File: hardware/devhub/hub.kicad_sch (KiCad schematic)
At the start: 32 parts, among them J2 USB-C UPSTREAM, U12 MCP120T-300I/TT, U2 USB2517I-JZX, Y1 24MHz 12pF

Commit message: Schematic: keep only host system LED, merge VBUS switches into hub sheet (D82, D83)
- remove relay LED (D90/R90) and power LED (D92/R92)
- move UCS2114 VBUS switches into the hub sheet, renamed to
  "Hub USB e switch VBUS"
- move the host LED into the MCU sheet as a local net
- drop the switches and ui sheets; update netclass patterns and docs
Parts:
- added C60, C63: 100n, Capacitor_SMD:C_0603_1608Metric, symbol Device:C
- added C61, C62, C64, C65: 1u 25V, Capacitor_SMD:C_0603_1608Metric, symbol Device:C
- added R60, R61: 27k 1%, Resistor_SMD:R_0603_1608Metric, symbol Device:R
- added R62, R63, R64, R65: 10k, Resistor_SMD:R_0603_1608Metric, symbol Device:R
- added U4, U5: UCS2114-1-V/LX, lcsc_footprints:UCS2114_VQFN-20_3x3mm_P0.5mm, symbol devhub:UCS2114
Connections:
- net +3V3: now also R62.1, R63.1, R64.1, R65.1
- net FAULT_P1: now also R62.2, U4.20 (~{ALERT1})
- net FAULT_P2: now also R63.2, U4.16 (~{ALERT2})
- net FAULT_P3: now also R64.2, U5.20 (~{ALERT1})
- net FAULT_P4: now also R65.2, U5.16 (~{ALERT2})
- net GND: now also C60.2, C61.2, C62.2, C63.2, C64.2, C65.2, R60.2, R61.2, U4.13 (~{BOOST}), U4.14 (GND), U4.17 (GND), U4.2 (GND), U5.13 (~{BOOST}), U5.14 (GND), U5.17 (GND), U5.2 (GND)
- net I2C1_SCL: now also U4.19 (SMCLK)
- net I2C1_SDA: now also U4.18 (SMDATA)
- new net +5V: C60.1, C61.1, C62.1, C63.1, C64.1, C65.1, U4.10 (VS), U4.6 (VS), U4.7 (VS), U4.8 (VDD), U4.9 (VS), U5.10 (VS), U5.6 (VS), U5.7 (VS), U5.8 (VDD), U5.9 (VS)
- new net EN_P1: U4.1 (PWR_EN1)
- new net EN_P2: U4.15 (PWR_EN2)
- new net EN_P3: U5.1 (PWR_EN1)
- new net EN_P4: U5.15 (PWR_EN2)
- new net I2C2_SCL: U5.19 (SMCLK)
- new net I2C2_SDA: U5.18 (SMDATA)
- new net ILIM_U4: R60.1, U4.3 (COMM_ILIM)
- new net ILIM_U5: R61.1, U5.3 (COMM_ILIM)
- new net VBUS_P1: U4.4 (VBUS1), U4.5 (VBUS1)
- new net VBUS_P2: U4.11 (VBUS2), U4.12 (VBUS2)
- new net VBUS_P3: U5.4 (VBUS1), U5.5 (VBUS1)
- new net VBUS_P4: U5.11 (VBUS2), U5.12 (VBUS2)
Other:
- note added: "Porte: 1-4 USB-C, 6 MCU (interna, non sezionabile); 5 e 7 non usate, disabilitate dal MCU via SMBus (con CFG_SEL 001 e 101 gli strap sono disattivati, D76). OCS1-4 dagli ALERT# degli UCS2114 (pull-up esterni R62-R65)."
- note added: "Switch VBUS delle porte: due UCS2114-1-V/LX (D75), U4 porte 1-2 su I2C1 e U5 porte 3-4 su I2C2, entrambi all'indirizzo 0x57. COMM_ILIM 27 k 1 %: modo SMBus, PWR_EN attivi alti, limite ILIM7 2,50-2,90 A per porta. Scarica VBUS automatica abilitata dal MCU all'avvio via SMBus (EN_VBUS_DISCHG, 400 ms): nessun GPIO di scarica. ALERT# open-drain con pull-up 10 k a 3,3 V: al MCU (FAULT_Px) e agli OCS1-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"
- note removed: "Porte: 1-4 USB-C, 6 MCU (interna, non sezionabile); 5 e 7 non usate, disabilitate dal MCU via SMBus (con CFG_SEL 001 e 101 gli strap sono disattivati, D76). OCS1-4 dagli ALERT# degli UCS2114 (pull-up esterni, foglio switches)."
- title: Hub USB 2.0 a 7 porte (USB2517) e porta upstream -> Hub USB2517, upstream e switch VBUS UCS2114

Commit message: PCB routing complete, package in values, MPN fields
- Routing finished; ESD_FANOUT rule area for D20 centre pins
- Vias keep inner-layer rings only where connected; GND reference vias
  next to SWD and I2C layer changes
- Value field of chip R/C/LED includes the package (0402...1206)
- New fields MPN lcsc, MPN mouser, MPN digikey; LCSC codes for R60/R61,
  U3, U4/U5 and supplier codes completed; JP2 marked DNP on the PCB
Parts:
- C20: value 4.7u -> 4.7u 0805; MPN digikey (none) -> CL21A475KOFNNNE; MPN lcsc (none) -> CL21A475KOFNNNE; MPN mouser (none) -> CL21A475KOFNNNE
- C21, C31, C32, C33, C35: value 1u -> 1u 0603; MPN digikey (none) -> CL10B105KA8NNNC; MPN lcsc (none) -> CL10B105KA8NNNC; MPN mouser (none) -> CL10B105KA8NNNC
- C22, C23: value 15p C0G -> 15p C0G 0603; MPN digikey (none) -> CL10C150JB8NNNC; MPN lcsc (none) -> CL10C150JB8NNNC; MPN mouser (none) -> CL10C150JB8NNNC
- C24, C60, C63: value 100n -> 100n 0603; MPN digikey (none) -> CL10B104KB8NNNC; MPN lcsc (none) -> CL10B104KB8NNNC; MPN mouser (none) -> CL10B104KB8NNNC
- C25, C26, C27, C28, C29, C30, C37, C38: value 100n -> 100n 0402; MPN digikey (none) -> CC0402KRX7R7BB104; MPN lcsc (none) -> CC0402KRX7R7BB104; MPN mouser (none) -> CC0402KRX7R7BB104
- C61, C62, C64, C65: value 1u 25V -> 1u 25V 0603; MPN digikey (none) -> CL10B105KA8NNNC; MPN lcsc (none) -> CL10B105KA8NNNC; MPN mouser (none) -> CL10B105KA8NNNC
- D20: MPN digikey (none) -> USBLC6-2SC6; MPN lcsc (none) -> USBLC6-2SC6; MPN mouser (none) -> USBLC6-2SC6
- J2: MPN digikey (none) -> USB4105-GF-A; MPN lcsc (none) -> USB4105-GF-A; MPN mouser (none) -> USB4105-GF-A
- R20, R21: value 5.1k -> 5.1k 0603; MPN digikey (none) -> RC0603FR-075K1L; MPN lcsc (none) -> 0603WAF5101T5E; MPN mouser (none) -> RC0603FR-075K1L
- R22, R23: value 100k -> 100k 0603; MPN digikey (none) -> RC0603FR-07100KL; MPN lcsc (none) -> FRC0603F1003TS; MPN mouser (none) -> RC0603FR-07100KL
- R24: value 1M -> 1M 0603; MPN digikey (none) -> RC0603FR-071ML; MPN lcsc (none) -> FRC0603F1004TS; MPN mouser (none) -> RC0603FR-071ML
- R25: value 12.0k 1% -> 12.0k 1% 0603; MPN digikey (none) -> RC0603FR-0712KL; MPN lcsc (none) -> RC0603FR-0712KL; MPN mouser (none) -> RC0603FR-0712KL
- R26, R27, R28, R29, R62, R63, R64, R65: value 10k -> 10k 0603; MPN digikey (none) -> RC0603FR-0710KL; MPN lcsc (none) -> FRC0603F1002TS; MPN mouser (none) -> RC0603FR-0710KL
- R60, R61: value 27k 1% -> 27k 1% 0603; MPN digikey (none) -> RC0603FR-0727KL; MPN lcsc (none) -> RC0603FR-0727KL; MPN mouser (none) -> RC0603FR-0727KL; lcsc (none) -> C114614
- U12: MPN digikey (none) -> MCP120T-300I/TT; MPN lcsc (none) -> MCP120T-300I/TT; MPN mouser (none) -> MCP120T-300I/TT
- U2: MPN digikey (none) -> USB2517I-JZX; MPN lcsc (none) -> USB2517I-JZX; MPN mouser (none) -> USB2517I-JZX
- U4, U5: MPN digikey (none) -> UCS2114-1-V/LX; MPN lcsc (none) -> UCS2114-1-V/LX; MPN mouser (none) -> UCS2114-1-V/LX; digikey (none) -> UCS2114-1-V/LX-ND; lcsc (none) -> C635426; mouser (none) -> 579-UCS2114-1-V/LX
- Y1: MPN digikey (none) -> ECS-240-12-33Q-JES-TR; MPN lcsc (none) -> X322524MOB4SI; MPN mouser (none) -> ECS-240-12-33Q-JES-TR

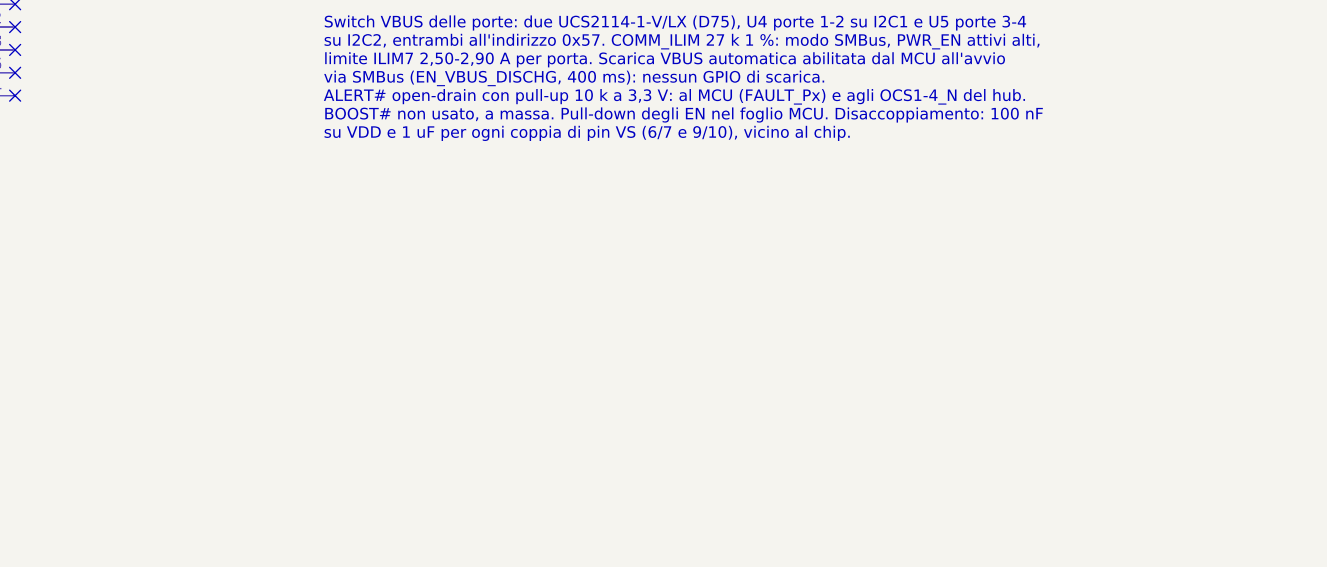
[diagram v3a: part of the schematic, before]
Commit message: Test points, LED host moved, board finished (D92)
- 14 test points: GND loops TP1/TP10 (Keystone 5001), pads for +5V, +3V3,
  I2C1/I2C2, HUB_RST_N, EFUSE_FLT_N and VBUS_P1-P4
- D93/R93 moved to the rear, left of J1
- Button symbols: generic Value, function in Description; PCB aligned
- Docs: decision D92, components, PCB test rules, LED host position
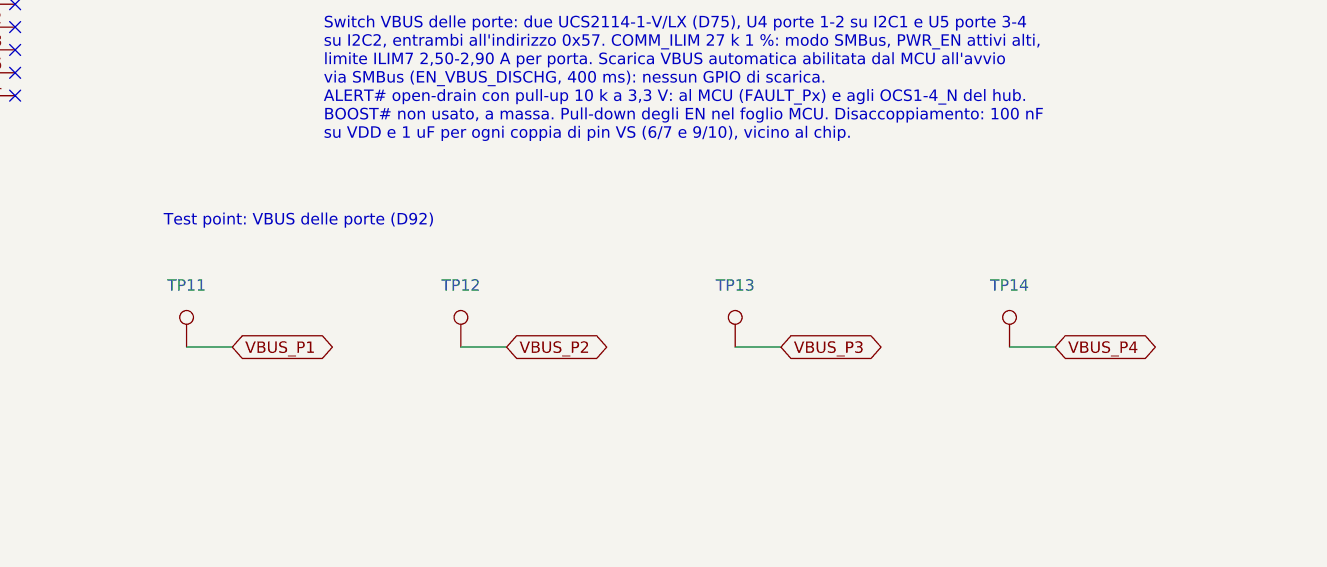
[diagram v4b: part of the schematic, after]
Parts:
- added TP11: VBUS_P1, TestPoint:TestPoint_Pad_D1.5mm, symbol Connector:TestPoint
- added TP12: VBUS_P2, TestPoint:TestPoint_Pad_D1.5mm, symbol Connector:TestPoint
- added TP13: VBUS_P3, TestPoint:TestPoint_Pad_D1.5mm, symbol Connector:TestPoint
- added TP14: VBUS_P4, TestPoint:TestPoint_Pad_D1.5mm, symbol Connector:TestPoint
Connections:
- net VBUS_P1: now also TP11.1
- net VBUS_P2: now also TP12.1
- net VBUS_P3: now also TP13.1
- net VBUS_P4: now also TP14.1
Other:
- note added: "Test point: VBUS delle porte (D92)"
